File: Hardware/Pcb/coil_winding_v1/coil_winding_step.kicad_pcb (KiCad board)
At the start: 2 copper layers, 20 parts, among them J1 Conn_01x14_Pin, J2 Screw_Terminal_01x02, SW1 SW_SPST, SW2 SW_SPST, SW3 RotaryEncoder_Switch, U1 LM7805_TO220

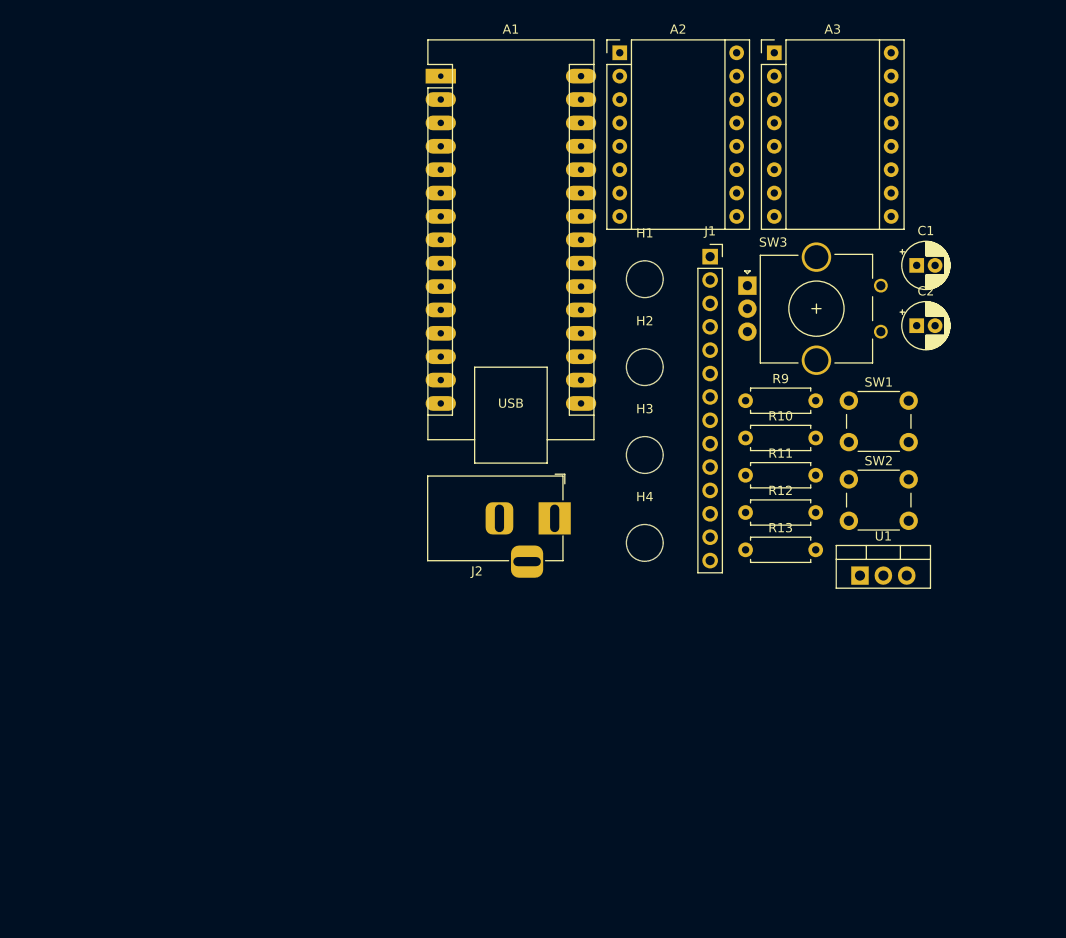
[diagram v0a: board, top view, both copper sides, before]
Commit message: Update version-2 PCB: modified tracks and footprint
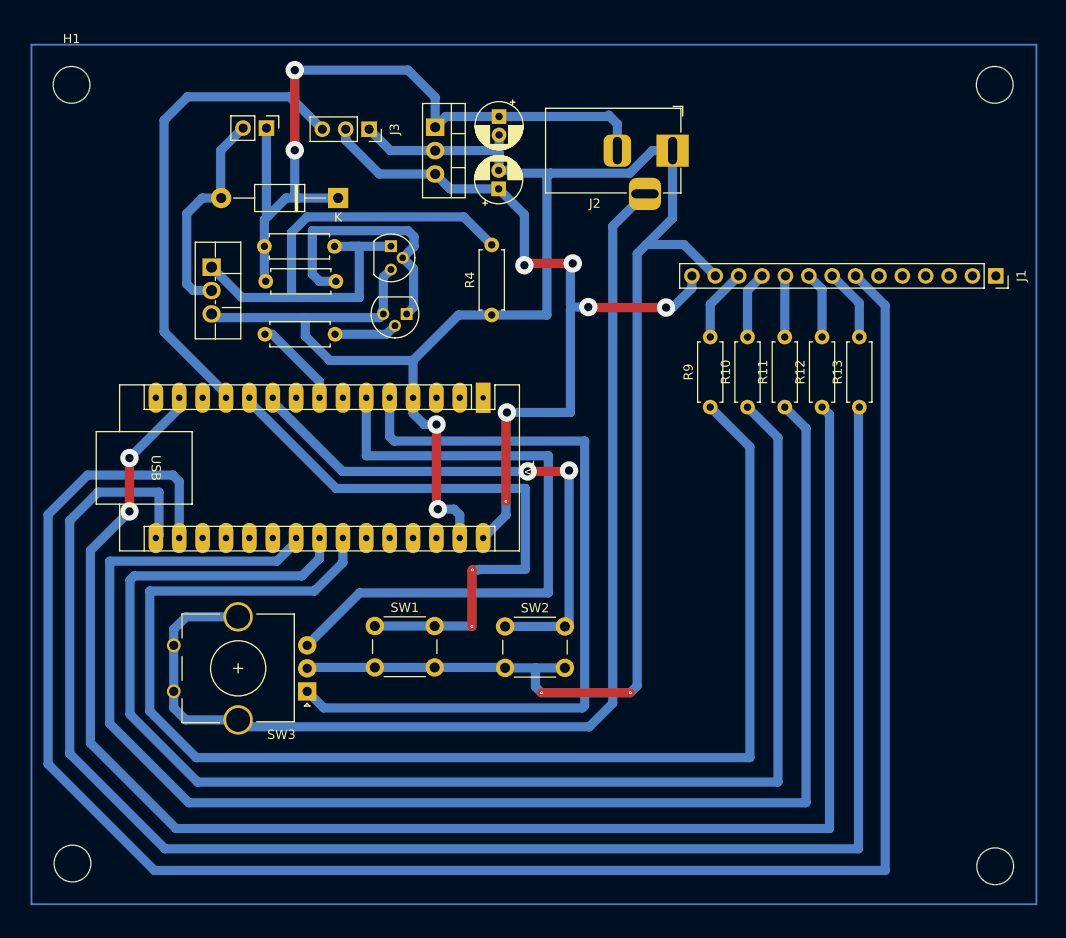
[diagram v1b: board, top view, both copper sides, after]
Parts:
- removed A2, A3: Pololu_Breakout_A4988, Module:Pololu_Breakout-16_15.2x20.3mm
- added D1: D, Diode_THT:D_DO-41_SOD81_P12.70mm_Horizontal, F.Cu at (131.5, 69.1)
- added J3: Conn_01x03_Socket, Connector_PinSocket_2.54mm:PinSocket_1x03_P2.54mm_Vertical, F.Cu at (134.9, 61.6)
- added M1: Motor_DC, Connector_PinHeader_2.54mm:PinHeader_1x02_P2.54mm_Vertical, F.Cu at (123.7, 61.5)
- added Q1: NPN, Package_TO_SOT_THT:TO-92, F.Cu at (139.0, 81.7)
- added Q2: NPN, Package_TO_SOT_THT:TO-92, F.Cu at (137.3, 74.3)
- added Q3: IRLIZ44N, Package_TO_SOT_THT:TO-220F-3_Vertical, F.Cu at (117.8, 76.6)
- added R1: R_US, Resistor_THT:R_Axial_DIN0207_L6.3mm_D2.5mm_P7.62mm_Horizontal, F.Cu at (123.6, 83.9)
- added R2: R_US, Resistor_THT:R_Axial_DIN0207_L6.3mm_D2.5mm_P7.62mm_Horizontal, F.Cu at (131.3, 78.1)
- added R3: R_US, Resistor_THT:R_Axial_DIN0207_L6.3mm_D2.5mm_P7.62mm_Horizontal, F.Cu at (131.1, 74.3)
- added R4: R_US, Resistor_THT:R_Axial_DIN0207_L6.3mm_D2.5mm_P7.62mm_Horizontal, F.Cu at (148.2, 81.8)
- moved H3 76.4 mm to (102.7, 141.4)
- moved U1 67.1 mm to (142.1, 61.4), turned to -90 degrees
- moved H1 65.8 mm to (102.6, 56.8)
- moved SW3 65.0 mm to (128.2, 122.7), turned to 180 degrees
- moved SW1 57.0 mm to (135.5, 115.6)
- moved H4 51.8 mm to (202.9, 141.7)
- moved H2 48.8 mm to (202.9, 56.8)
- moved C1 48.2 mm to (149.0, 60.2), turned to -90 degrees
- moved C2 47.8 mm to (149.0, 68.1), turned to 90 degrees
- moved J2 42.0 mm to (167.9, 63.9)
- moved SW2 40.6 mm to (149.7, 115.6)
- moved A1 35.2 mm to (147.3, 90.8), turned to -90 degrees
- moved J1 31.1 mm to (203.0, 77.5), turned to -90 degrees
- moved R13 19.8 mm to (188.2, 91.8), turned to 90 degrees
- moved R12 14.1 mm to (184.1, 91.8), turned to 90 degrees
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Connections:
- A1 pad 15: D12 -> unconnected-(A1-D12-Pad15)
- A1 pad 9: D6 -> unconnected-(A1-D6-Pad9)
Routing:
- net GND: track 0.00 -> 244.4 mm, vias 0 -> 4
- net 3V3: track 0.00 -> 211.2 mm
- net D13: track 0.00 -> 179.4 mm
- net D11: track 0.00 -> 171.8 mm, vias 0 -> 2
- net A3: track 0.00 -> 162.3 mm
- net A4: track 0.00 -> 153.9 mm
- net A5: track 0.00 -> 146.0 mm
- net (no net): track 0.00 -> 122.5 mm
- net +5V: track 0.00 -> 88.1 mm, vias 0 -> 6
- net D2: track 0.00 -> 85.4 mm
- net VCC: track 0.00 -> 82.8 mm, vias 0 -> 2
- net D3: track 0.00 -> 69.5 mm
- net D8: track 0.00 -> 65.6 mm, vias 0 -> 2
- net Net-(Q2-C): track 0.00 -> 60.8 mm
- net D7: track 0.00 -> 59.4 mm, vias 0 -> 2
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
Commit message: Changes made
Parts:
- SW3: footprint Rotary_Encoder:RotaryEncoder_Alps_EC11E_Vertical_H20mm_CircularMountingHoles -> Rotary_Encoder:RotaryEncoder_Alps_EC12E-Switch_Vertical_H20mm
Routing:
- net D4: track 0.00 -> 123.6 mm, vias 0 -> 4
- net (no net): track 122.5 -> 0.00 mm
- net GND: track 244.4 -> 262.5 mm
- net D2: track 85.4 -> 89.4 mm
- net A5: track 146.0 -> 147.2 mm

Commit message: slight changes
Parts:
- removed Q1, Q2: NPN, Package_TO_SOT_THT:TO-92
- removed R3: R_US, Resistor_THT:R_Axial_DIN0207_L6.3mm_D2.5mm_P7.62mm_Horizontal
- added J4: Conn_01x03_Socket, Connector_PinHeader_2.54mm:PinHeader_1x03_P2.54mm_Vertical, F.Cu at (139.5, 72.6)
- Q3: value IRLIZ44N -> IRFZ40
- R1: value R_US -> 220
- R2: value R_US -> 10K
- moved J2 10.1 mm to (177.8, 65.0), turned to 180 degrees
- moved R2 5.24 mm to (126.5, 76.0), turned to 0 degrees
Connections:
- A1 pad 9: unconnected-(A1-D6-Pad9) -> D6
- Q3 pad 1: Net-(Q2-C) -> Net-(Q3-G)
- R1 pad 2: Net-(Q1-B) -> Net-(Q3-G)
- R2 pad 1: Net-(Q1-C) -> GND
- R2 pad 2: VCC -> Net-(Q3-G)
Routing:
- net D6: track 0.00 -> 89.1 mm, vias 0 -> 4
- net Net-(Q2-C): track 60.8 -> 0.00 mm
- net Net-(Q3-G): track 0.00 -> 29.1 mm
- net Net-(Q1-C): track 28.6 -> 0.00 mm
- net GND: track 262.5 -> 287.0 mm
- net VCC: track 82.8 -> 100.6 mm
- net Net-(D1-A): track 24.1 -> 41.4 mm
- net +5V: track 88.1 -> 100.2 mm
- net D9: track 52.6 -> 61.8 mm
- net Net-(Q1-B): track 6.90 -> 0.00 mm
- net D7: track 59.4 -> 65.1 mm
- net D8: track 65.6 -> 70.7 mm
- net D11: track 171.8 -> 175.8 mm
- net D2: track 89.4 -> 93.3 mm
- net D4: track 123.6 -> 126.9 mm
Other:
- board outline added: 111.8 x 96.4 mm

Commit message: tuesday
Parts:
- removed J4: Conn_01x03_Socket, Connector_PinHeader_2.54mm:PinHeader_1x03_P2.54mm_Vertical
- removed R4: R_US, Resistor_THT:R_Axial_DIN0207_L6.3mm_D2.5mm_P7.62mm_Horizontal
- added J5: Conn_01x04_Socket, Connector_PinHeader_2.54mm:PinHeader_1x04_P2.54mm_Vertical, F.Cu at (155.0, 72.7)
- moved SW3 34.5 mm to (156.1, 102.5)
- moved SW2 24.2 mm to (131.1, 100.1), turned to 180 degrees
- moved SW1 23.3 mm to (118.0, 100.2), turned to 180 degrees
- moved A1 19.0 mm to (148.9, 109.7)
- moved D1 14.9 mm to (124.2, 56.1), turned to -90 degrees
- moved R1 14.1 mm to (135.8, 91.0), turned to 90 degrees
- moved R2 12.4 mm to (132.2, 87.0), turned to 90 degrees
- moved R13 9.25 mm to (193.7, 84.4), turned to 180 degrees
- moved J2 7.99 mm to (185.8, 65.5)
- moved C1 6.42 mm to (154.9, 57.7)
- moved C2 5.78 mm to (154.7, 67.2)
- moved Q3 5.62 mm to (122.6, 79.5)
- moved M1 4.98 mm to (118.8, 61.7)
- moved H3 4.02 mm to (101.2, 137.7)
- moved H4 3.99 mm to (204.0, 137.8)
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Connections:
- A1 pad 19: unconnected-(A1-A0-Pad19) -> A0
- A1 pad 30: +5V -> unconnected-(A1-VIN-Pad30)
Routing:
- net A0: track 0.00 -> 217.3 mm, vias 0 -> 2
- net D4: track 126.9 -> 12.8 mm, vias 4 -> 0
- net GND: track 287.0 -> 204.8 mm, vias 4 -> 0
- net D11: track 175.8 -> 97.5 mm
- net 3V3: track 211.2 -> 135.4 mm
- net A5: track 147.2 -> 74.3 mm
- net A4: track 153.9 -> 84.4 mm
- net A3: track 162.3 -> 95.1 mm
- net D2: track 93.3 -> 30.4 mm
- net D8: track 70.7 -> 11.8 mm, vias 2 -> 0
- net D7: track 65.1 -> 10.2 mm, vias 2 -> 0
- net D3: track 70.0 -> 27.3 mm
- net D13: track 179.4 -> 140.2 mm
- net +5V: track 100.2 -> 133.9 mm, vias 6 -> 2
- net D9: track 61.8 -> 78.2 mm, vias 0 -> 2
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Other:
- board size 111.8 x 96.4 mm -> 111.8 x 91.3 mm
